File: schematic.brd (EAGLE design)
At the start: 160 x 100 mm, 56 parts, among them J1 FTDI_DEVICERA_SMT, M1 WIRELESS-NRF24L01, Q1 8MHz, T1 NMOS, T2 NMOS, T3 NMOS, T4 NMOS, U1 ATMEGA328P_TQFP, U2 GY-521MPU6050, U3 TPS63060

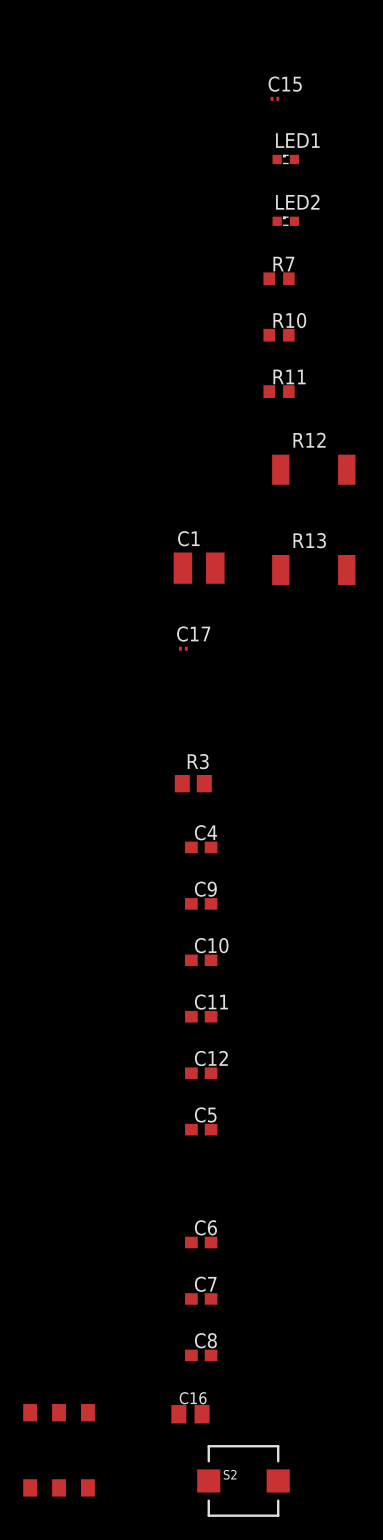
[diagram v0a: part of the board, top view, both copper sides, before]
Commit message: Removed switch, changed some names, removed an unnecessary capacitor
Changed power from battery to PWR instead of VCC, to be exact
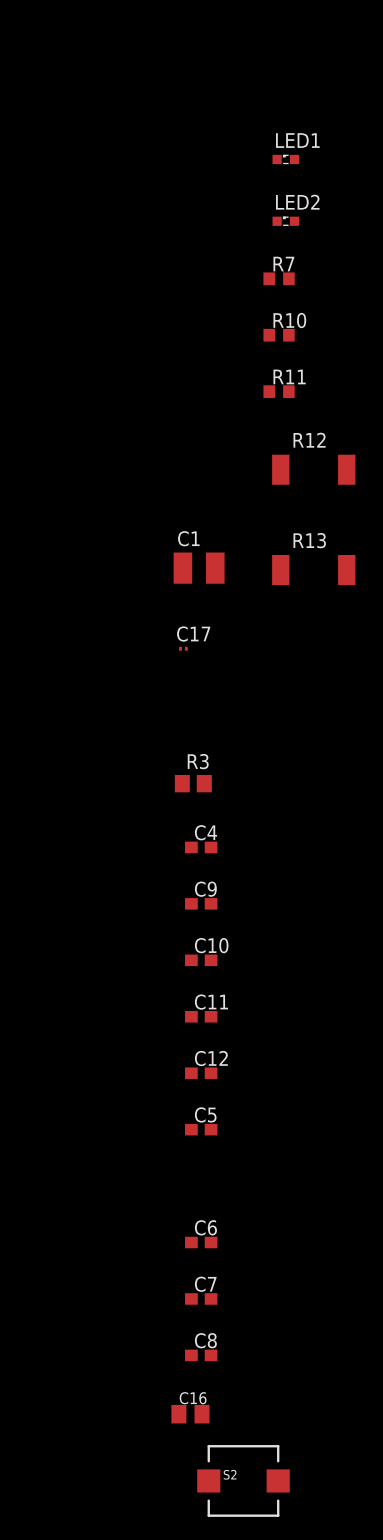
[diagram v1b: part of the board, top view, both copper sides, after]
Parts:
- removed C15: 0.1uF, resistor:C0201
- removed S1: SLIDING_SWITCH, wurth:SLIDE_SWITCH
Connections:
- removed net N$8: S1.P$5, U$1.+
- removed net VCC: C1.1, C2.1, C3.1, D1.NEG, D2.NEG, D3.NEG, D4.NEG, R1.1, R2.2, S1.P$6, U$10.+, U$13.+, U$4.+, U$7.+, U3.2, U3.3
- new net PWR: C1.1, C2.1, C3.1, D1.NEG, D2.NEG, D3.NEG, D4.NEG, R1.1, R2.2, U$1.+, U$10.+, U$13.+, U$4.+, U$7.+, U3.2, U3.3
- net GND: no longer C15.2
- net V_REG_OUT: no longer C15.1
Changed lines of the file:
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@@
 <attribute name="SPICEPREFIX" value="R" x="-71.034909375" y="-41.91048125" size="0.1" layer="27" display="off"/>
 </element>
-<element name="C15" library="resistor" library_urn="urn:adsk.eagle:library:348" package="C0201" package3d_urn="urn:adsk.eagle:package:26209/1" value="0.1uF" x="-71.39030625" y="-71.17128125"/>
 <element name="LED1" library="led" library_urn="urn:adsk.eagle:library:259" package="SML0603" package3d_urn="urn:adsk.eagle:package:15832/1" value="RED" x="-70.45" y="-76.41308125"/>
 <element name="LED2" library="led" library_urn="urn:adsk.eagle:library:259" package="SML0603" package3d_urn="urn:adsk.eagle:package:15832/1" value="RED" x="-70.45" y="-81.7499"/>
@@
 <element name="C16" library="resistor" library_urn="urn:adsk.eagle:library:348" package="C0805K" package3d_urn="urn:adsk.eagle:package:26201/1" value="10uF" x="-78.689225" y="-184.82673125"/>
 <element name="S2" library="adafruit" package="PUSHBUTTON_SMD_SJ" value="" x="-74.107496875" y="-190.594996875"/>
-<element name="S1" library="wurth" package="SLIDE_SWITCH" value="SLIDING_SWITCH" x="-90.045665625" y="-188.196575"/>
 </elements>
 <signals>
-<signal name="VCC">
-<contactref element="U3" pad="2"/>
-<contactref element="U3" pad="3"/>
-<contactref element="C2" pad="1"/>
-<contactref element="C3" pad="1"/>
-<contactref element="R2" pad="2"/>
-<contactref element="U$4" pad="+"/>
-<contactref element="D1" pad="NEG"/>
-<contactref element="U$7" pad="+"/>
-<contactref element="D2" pad="NEG"/>
-<contactref element="U$10" pad="+"/>
-<contactref element="D3" pad="NEG"/>
-<contactref element="U$13" pad="+"/>
-<contactref element="D4" pad="NEG"/>
-<contactref element="R1" pad="1"/>
-<contactref element="C1" pad="1"/>
-<contactref element="S1" pad="P$6"/>
-<wire x1="-87.545665625" y1="-191.196575" x2="-79.342440625" y2="-111.721646875" width="0" layer="19" extent="1-1"/>
-<wire x1="-71.884909375" y1="-29.01904375" x2="-79.342440625" y2="-111.721646875" width="0" layer="19" extent="1-1"/>
-<wire x1="-54.61" y1="56.88" x2="-71.884909375" y2="-29.01904375" width="0" layer="19" extent="1-1"/>
-<wire x1="-49.53" y1="56.88" x2="-54.61" y2="56.88" width="0" layer="19" extent="1-1"/>
-<wire x1="-44.45" y1="56.88" x2="-49.53" y2="56.88" width="0" layer="19" extent="1-1"/>
-<wire x1="-39.37" y1="56.88" x2="-44.45" y2="56.88" width="0" layer="19" extent="1-1"/>
-<wire x1="-59.42" y1="62.23" x2="-54.61" y2="56.88" width="0" layer="19" extent="1-1"/>
-<wire x1="-64.5" y1="62.23" x2="-59.42" y2="62.23" width="0" layer="19" extent="1-1"/>
-<wire x1="-67.31" y1="63.78" x2="-64.5" y2="62.23" width="0" layer="19" extent="1-1"/>
-<wire x1="-69.85" y1="63.78" x2="-67.31" y2="63.78" width="0" layer="19" extent="1-1"/>
-<wire x1="-25.09" y1="48.26" x2="-39.37" y2="56.88" width="0" layer="19" extent="1-1"/>
-<wire x1="-25.9" y1="67.105" x2="-39.37" y2="56.88" width="0" layer="19" extent="1-1"/>
-<wire x1="-25.4" y1="67.105" x2="-25.9" y2="67.105" width="0" layer="19" extent="1-1"/>
-<wire x1="-16.51" y1="70.13" x2="-25.4" y2="67.105" width="0" layer="19" extent="1-1"/>
-<wire x1="-13.97" y1="70.13" x2="-16.51" y2="70.13" width="0" layer="19" extent="1-1"/>
-</signal>
 <signal name="N$2">
 <contactref element="U1" pad="29"/>
@@
 <contactref element="C14" pad="2"/>
 <contactref element="R5" pad="1"/>
-<contactref element="C15" pad="2"/>
 <contactref element="LED1" pad="C"/>
 <contactref element="LED2" pad="C"/>
@@
 <wire x1="-71.2" y1="-81.7499" x2="-71.884909375" y2="-91.598521875" width="0" layer="19" extent="1-1"/>
 <wire x1="-71.2" y1="-76.41308125" x2="-71.2" y2="-81.7499" width="0" layer="19" extent="1-1"/>
-<wire x1="-71.14030625" y1="-71.17128125" x2="-71.2" y2="-76.41308125" width="0" layer="19" extent="1-1"/>
-<wire x1="-71.89030625" y1="-17.99544375" x2="-71.14030625" y2="-71.17128125" width="0" layer="19" extent="1-1"/>
+<wire x1="-71.89030625" y1="-17.99544375" x2="-71.2" y2="-76.41308125" width="0" layer="19" extent="1-1"/>
 <wire x1="-57.15" y1="16.51" x2="-71.89030625" y2="-17.99544375" width="0" layer="19" extent="1-1"/>
 <wire x1="-42.3926" y1="28.81" x2="-57.15" y2="16.51" width="0" layer="19" extent="1-1"/>
@@
 <contactref element="R4" pad="2"/>
 <contactref element="R6" pad="2"/>
-<contactref element="C15" pad="1"/>
 <contactref element="R7" pad="2"/>
 <contactref element="C17" pad="1"/>
@@
 <wire x1="-79.547834375" y1="-118.6854625" x2="-78.607503125" y2="-145.6094625" width="0" layer="19" extent="1-1"/>
 <wire x1="-70.184909375" y1="-86.721721875" x2="-79.547834375" y2="-118.6854625" width="0" layer="19" extent="1-1"/>
-<wire x1="-71.64030625" y1="-71.17128125" x2="-70.184909375" y2="-86.721721875" width="0" layer="19" extent="1-1"/>
-<wire x1="-70.184909375" y1="-33.316190625" x2="-71.64030625" y2="-71.17128125" width="0" layer="19" extent="1-1"/>
+<wire x1="-70.184909375" y1="-33.316190625" x2="-70.184909375" y2="-86.721721875" width="0" layer="19" extent="1-1"/>
 <wire x1="-69.5849125" y1="-23.50724375" x2="-70.184909375" y2="-33.316190625" width="0" layer="19" extent="1-1"/>
 <wire x1="-54.61" y1="16.51" x2="-69.5849125" y2="-23.50724375" width="0" layer="19" extent="1-1"/>
@@
 <wire x1="-45.3" y1="72.39" x2="-42.3926" y2="27.21" width="0" layer="19" extent="1-1"/>
 </signal>
-<signal name="N$8">
+<signal name="PWR">
+<contactref element="C1" pad="1"/>
+<contactref element="U3" pad="2"/>
+<contactref element="U3" pad="3"/>
+<contactref element="C2" pad="1"/>
+<contactref element="C3" pad="1"/>
+<contactref element="R2" pad="2"/>
+<contactref element="U$4" pad="+"/>
+<contactref element="D1" pad="NEG"/>
+<contactref element="U$7" pad="+"/>
+<contactref element="D2" pad="NEG"/>
+<contactref element="U$10" pad="+"/>
+<contactref element="D3" pad="NEG"/>
+<contactref element="U$13" pad="+"/>
+<contactref element="D4" pad="NEG"/>
+<contactref element="R1" pad="1"/>
 <contactref element="U$1" pad="+"/>
-<contactref element="S1" pad="P$5"/>
-<wire x1="-34.29" y1="56.88" x2="-90.045665625" y2="-191.196575" width="0" layer="19" extent="1-1"/>
+<wire x1="-71.884909375" y1="-29.01904375" x2="-79.342440625" y2="-111.721646875" width="0" layer="19" extent="1-1"/>
+<wire x1="-54.61" y1="56.88" x2="-71.884909375" y2="-29.01904375" width="0" layer="19" extent="1-1"/>
+<wire x1="-49.53" y1="56.88" x2="-54.61" y2="56.88" width="0" layer="19" extent="1-1"/>
+<wire x1="-44.45" y1="56.88" x2="-49.53" y2="56.88" width="0" layer="19" extent="1-1"/>
+<wire x1="-39.37" y1="56.88" x2="-44.45" y2="56.88" width="0" layer="19" extent="1-1"/>
+<wire x1="-34.29" y1="56.88" x2="-39.37" y2="56.88" width="0" layer="19" extent="1-1"/>
+<wire x1="-59.42" y1="62.23" x2="-54.61" y2="56.88" width="0" layer="19" extent="1-1"/>
+<wire x1="-64.5" y1="62.23" x2="-59.42" y2="62.23" width="0" layer="19" extent="1-1"/>
+<wire x1="-67.31" y1="63.78" x2="-64.5" y2="62.23" width="0" layer="19" extent="1-1"/>
+<wire x1="-69.85" y1="63.78" x2="-67.31" y2="63.78" width="0" layer="19" extent="1-1"/>
+<wire x1="-25.09" y1="48.26" x2="-34.29" y2="56.88" width="0" layer="19" extent="1-1"/>
+<wire x1="-25.9" y1="67.105" x2="-34.29" y2="56.88" width="0" layer="19" extent="1-1"/>
+<wire x1="-25.4" y1="67.105" x2="-25.9" y2="67.105" width="0" layer="19" extent="1-1"/>
+<wire x1="-16.51" y1="70.13" x2="-25.4" y2="67.105" width="0" layer="19" extent="1-1"/>
+<wire x1="-13.97" y1="70.13" x2="-16.51" y2="70.13" width="0" layer="19" extent="1-1"/>
 </signal>
 </signals>

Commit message: Fixed issues mentioned in design review
Changed voltage divider resistors to 10K.
Got new voltage regulator, completely circuit and PCD footprint.
Changed all component package to 0603.
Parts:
- removed C16: 10uF, resistor:C0805K
- removed C17: 0.1uF, resistor:C0201
- added C15: 0.1uF, resistor:C0603
- added R14: 10K, resistor:R0603
- added R15, R16: 10K, resistor:M2309
- C12: value 0.1uF -> 27pF; device rcl:C0603 -> resistor:C0603
- C14: value 27pF -> 10uF
- C2: value 10uF -> 0.056uF; device resistor:C0805K -> resistor:C0603
- C3: device resistor:C0805K -> resistor:C0603
- C4: value 0.1uF -> 100pF; device rcl:C0603 -> resistor:C0603
- C5: value 10pF -> 22uF; device rcl:C0603 -> resistor:C0603
- C6: value 22uF -> 470pF; device rcl:C0603 -> resistor:C0603
- C7: value 22uF -> 10pF; device rcl:C0603 -> resistor:C0603
- C8: value 22uF -> 0.1uF
- L1: value 1uH -> 3.3uH
- R11: value 10K -> 820; device resistor:R0603 -> rcl:R0603
- R12: value 10K -> 820; device resistor:M2309 -> rcl:R0603
- R13: device resistor:M2309 -> resistor:R0603
- R2: value 50K -> 10K; device resistor:M2309 -> resistor:R0603
- R3: value 150K -> 10K; device resistor:R0805 -> resistor:R0603
- R4: value 560K -> 200K; device rcl:R0805 -> resistor:R0603
- R5: value 100K -> 10K; device rcl:R0402 -> resistor:R0603
- R6: value 820 -> 374K; device rcl:R0603 -> resistor:R0603
- R7: value 10K -> 15K
- R8: value 820 -> 162K; device rcl:R0603 -> resistor:R0603
- S2: value (none) -> PUSH_BUTTON
- U3: value TPS63060 -> LTC3534; device SparkFun-PowerIC:QFN-10_PAD-8 -> LTC3534:SSOP-16GN
- moved C8 269.0 mm to (-182.1, 68.2)
- moved C5 268.0 mm to (-254.7, 41.0)
- moved C6 260.8 mm to (-254.7, 21.5)
- moved C7 260.8 mm to (-254.7, 16.7)
- moved C4 253.7 mm to (-254.7, 45.9)
- moved R13 253.1 mm to (-175.4, 117.3)
- moved C14 240.6 mm to (-254.7, -18.0)
- moved R10 237.9 mm to (-175.4, 122.2)
- moved C1 233.5 mm to (-182.3, 97.2)
- moved LED2 233.5 mm to (-174.8, 127.2)
- moved S2 233.5 mm to (-178.4, 18.3)
- moved R2 230.9 mm to (-255.9, 11.8)
- moved C12 230.2 mm to (-44.5, 72.4)
- moved C10 229.2 mm to (-182.1, 58.4)
- moved C11 229.2 mm to (-182.1, 53.6)
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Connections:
- removed net N$27: L1.1, U3.1
- removed net N$28: L1.2, U3.10
- removed net N$32: C5.1, R4.1, R5.2, U3.8
- removed net N$33: C4.1, U3.6
- new net N$15: C4.1, R5.1
- new net N$16: C2.1, R4.1, U3.2
- new net N$18: C4.2, C7.2, R6.1, R7.1, R8.2, U3.15
- new net N$19: C6.1, C7.1, U3.14
- new net N$20: C6.2, R7.2
- new net N$8: L1.1, U3.5
- new net N$9: L1.2, U3.6
- net DEBUG_LED1: now also R12.2; no longer R9.2
- net DEBUG_LED2: now also R11.2; no longer R8.2
- net DTR: now also C8.1; no longer C9.1
- net GND: now also C15.2, C9.2, R13.1, R14.1, R15.2, R16.2, R8.1, U3.1, U3.3, U3.8, U3.9; no longer C16.2, C17.2, C4.2, C6.2, C7.2, C8.2, R10.1, R11.1, R12.2, R13.2, R5.1, U3.11, U3.12, U3.13, U3.14, U3.15, U3.17, U3.18, U3.PAD
- net N$1: now also C12.1; no longer C13.1
- net N$11: now also R9.1; no longer R6.1
- net N$12: now also R12.1; no longer R9.1
- net N$13: now also R11.1; no longer R8.1
- net N$2: now also C8.2, R10.1; no longer C9.2, R7.1
- net N$25: now also C11.1; no longer C12.1
- net N$4: now also C13.1; no longer C14.1
- net PWM1: now also R13.2; no longer R10.2
- net PWM2: now also R14.2; no longer R11.2
- net PWM3: now also R15.1; no longer R12.1
- net PWM4: now also R16.1; no longer R13.1
- net PWR: now also R4.2, U3.10, U3.12, U3.13; no longer C2.1, U3.2, U3.3
- net V_REG_OUT: now also C14.1, C15.1, C5.1, C9.1, R10.2, R5.2, R9.2, U3.11; no longer C11.1, C16.1, C17.1, C6.1, C7.1, C8.1, R4.2, R7.2, U3.9
